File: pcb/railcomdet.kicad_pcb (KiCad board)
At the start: 4 copper layers, 90 x 70 mm, 161 parts, among them J1 MVE252-5-V, J10 MVE252-5-V, J2 MVE252-5-V, J3 MVE252-5-V, J4 MVE252-5-V, J5 MVE252-5-V, J6 PINHEADER, J7 PINHEADER, J8 PROG/DEBUG, J9 MVE252-5-V, SW1 6x6, U1 VO0631T, U10 LM339, U11 LM339, U12 STM32F103C8Tx, U13 AMS1117-3.3, U14 L78L05_SOT89, U15 SN75176AP, U2 VO0631T, U3 VO0631T, U4 L78L05_SOT89, U5 L79L05_SOT89, U6 LM339, U7 LM339, U8 LM339, U9 4052, Y1 14,7456MHz

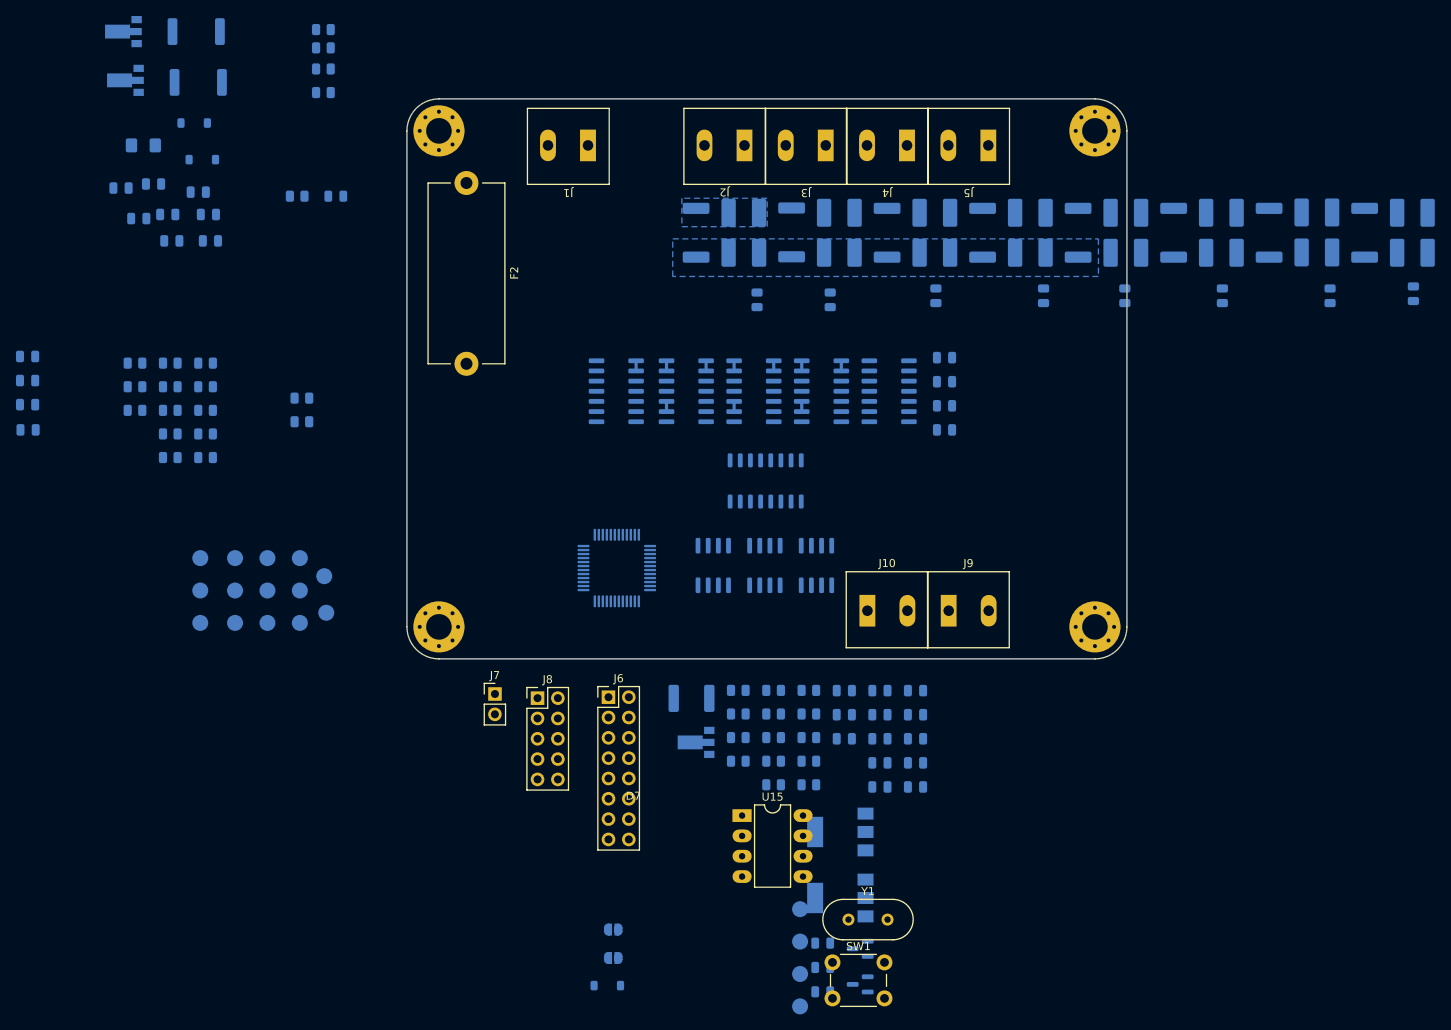
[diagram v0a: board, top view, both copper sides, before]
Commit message: pcb: wire multiplexors.
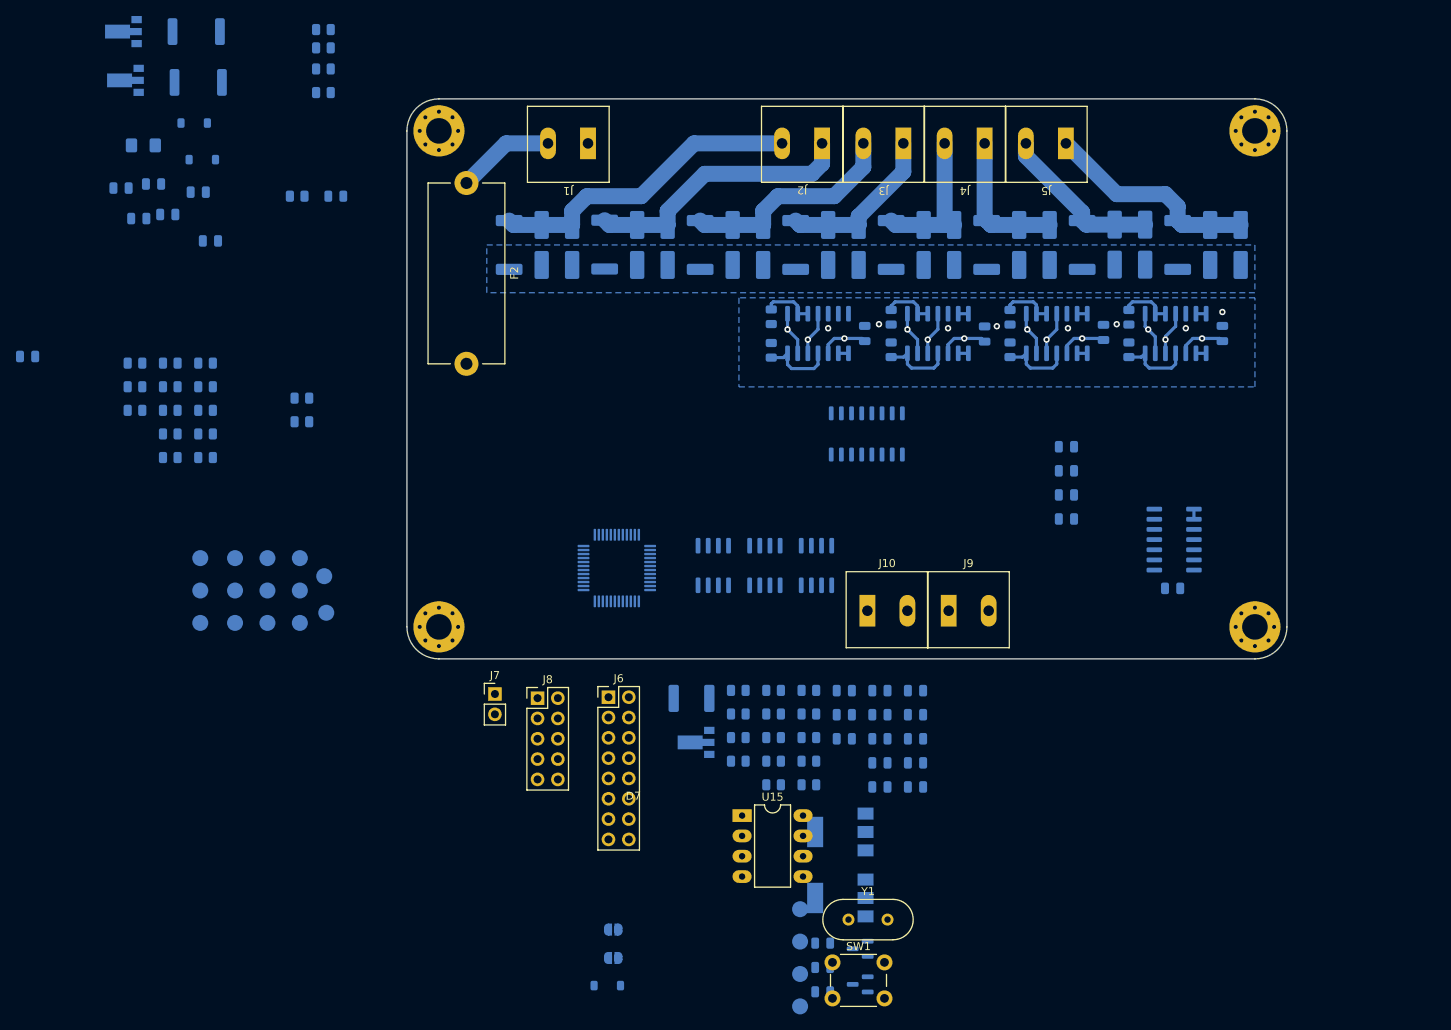
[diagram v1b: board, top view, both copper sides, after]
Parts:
- moved C15 149.6 mm to (201.9, 59.3), turned to 90 degrees
- moved C16 144.4 mm to (195.7, 91.2)
- moved C14 134.6 mm to (187.1, 59.2), turned to 90 degrees
- moved C12 102.3 mm to (172.2, 59.4), turned to 90 degrees
- moved C11 83.4 mm to (157.2, 59.3), turned to 90 degrees
- moved U11 72.1 mm to (195.9, 85.1)
- moved U10 61.6 mm to (196.1, 59.3), turned to 90 degrees
- moved U8 38.5 mm to (181.2, 59.3), turned to 90 degrees
- moved R34 35.7 mm to (190.2, 57.3), turned to 90 degrees
- moved R32 26.7 mm to (175.4, 57.3), turned to 90 degrees
- moved R33 26.0 mm to (190.2, 61.4)
- moved D19 23.4 mm to (168.4, 48.3)
- moved D24 23.4 mm to (188.5, 48.2)
- moved R16 23.4 mm to (136.7, 48.3)
- moved R14 23.4 mm to (112.8, 48.3)
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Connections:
- R29 pad 2: Net-(U8A--) -> Net-(U11A--)
- R30 pad 1: Net-(U8A--) -> Net-(U11A--)
- R31 pad 2: Net-(U10A--) -> Net-(U8A--)
- R33 pad 2: Net-(U11A--) -> Net-(U10A--)
- U10 pad 1: Net-(U9-Y3) -> Net-(U9-Y1)
- U10 pad 2: Net-(U9-Y3) -> Net-(U9-Y1)
- U11 pad 1: Net-(U9-Y1) -> /DCC/CUTOUT
- U11 pad 2: Net-(U9-Y1) -> /DCC/CUTOUT
- U8 pad 1: /DCC/CUTOUT -> Net-(U9-Y3)
- U8 pad 2: /DCC/CUTOUT -> Net-(U9-Y3)
- U8 pad 5: REF- -> REF+
- U8 pad 6: REF+ -> REF-
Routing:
- net REF-: track 0.00 -> 72.3 mm, vias 0 -> 4
- net REF+: track 0.00 -> 71.1 mm, vias 0 -> 4
- net /DCC/J1: track 0.00 -> 39.6 mm
- net /DCC/J2: track 0.00 -> 34.2 mm
- net /DCC/J3: track 0.00 -> 27.6 mm
- net /DCC/J8: track 0.00 -> 27.1 mm
- net +5VA: track 0.00 -> 24.3 mm, vias 0 -> 4
- net /DCC/J7: track 0.00 -> 20.6 mm
- net /DCC/J4: track 0.00 -> 20.6 mm
- net /DCC/J5: track 0.00 -> 18.3 mm
- net /DCC/J6: track 0.00 -> 17.9 mm
- net /DCC/J: track 0.00 -> 12.2 mm
- net /DCC/RC1: track 0.00 -> 9.28 mm
- net Net-(U8A--): track 0.00 -> 9.13 mm
- net Net-(U7A--): track 0.00 -> 9.13 mm
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- added copper zone on In1.Cu, net +5VA
- added copper zone on B.Cu, net -5VA
- added copper zone on In2.Cu, net -5VA
- removed copper zone on B.Cu, net /DCC/J1
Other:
- board size 90 x 70 mm -> 110 x 70 mm

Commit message: pcb: wire dcc voltage stabilization.
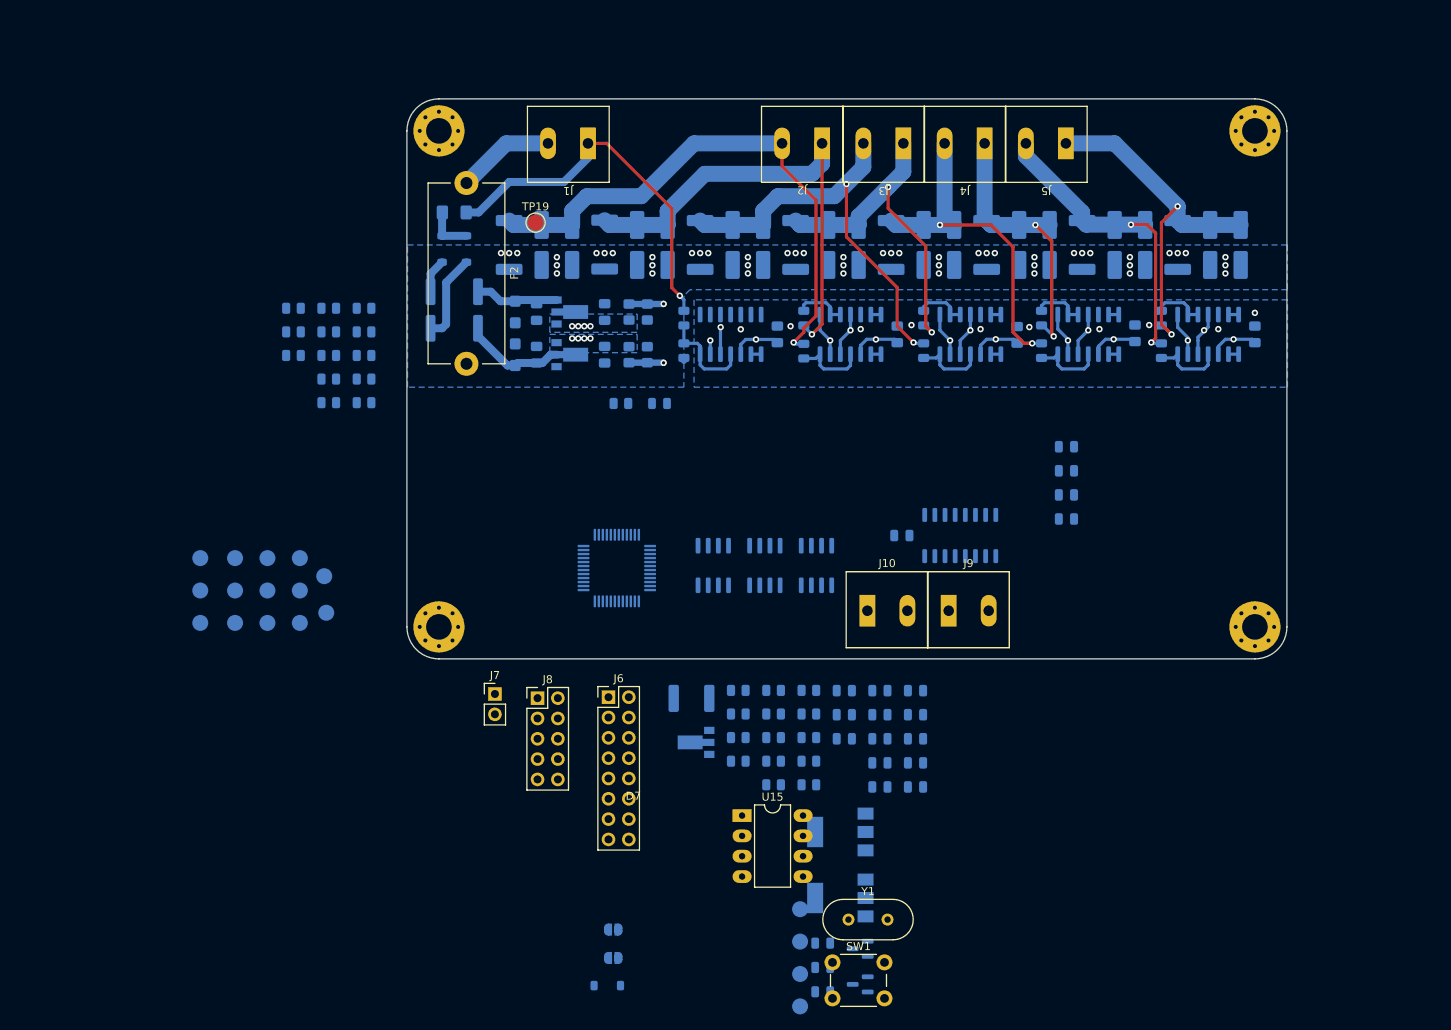
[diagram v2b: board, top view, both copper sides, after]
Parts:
- added TP19: PAD, TestPoint:TestPoint_Pad_D2.0mm, F.Cu at (116.1, 45.5)
- C10, C11, C12, C14, C15, C16, C7, C8, C9: footprint Capacitor_SMD:C_0805_2012Metric -> Capacitor_SMD:C_0805_2012Metric_Pad1.18x1.45mm_HandSolder
- C5, C6: footprint Capacitor_SMD:C_0805_2012Metric -> Capacitor_Tantalum_SMD:CP_EIA-3216-10_Kemet-I
- D1, D2: value 1N5819WS -> 1N5819
- R24, R25, R26, R27: footprint Resistor_SMD:R_0805_2012Metric -> Resistor_SMD:R_0805_2012Metric_Pad1.20x1.40mm_HandSolder
- moved C13 111.5 mm to (161.9, 84.6)
- moved U4 66.4 mm to (120.7, 56.6), turned to 0 degrees
- moved U5 65.8 mm to (120.7, 62.0), turned to 0 degrees
- moved U11 61.1 mm to (140.5, 59.4), turned to 90 degrees
- moved C16 58.7 mm to (146.3, 59.4), turned to 90 degrees
- moved C9 58.6 mm to (124.7, 56.6), turned to 90 degrees
- moved C10 57.4 mm to (124.7, 62.0), turned to 90 degrees
- moved R26 54.0 mm to (130.0, 62.0), turned to -90 degrees
- moved R25 52.2 mm to (130.0, 56.6), turned to -90 degrees
- moved R24 52.0 mm to (127.8, 56.6), turned to 90 degrees
- moved C5 51.7 mm to (113.5, 56.6), turned to -90 degrees
- moved C7 51.1 mm to (116.2, 56.6), turned to -90 degrees
- moved R27 50.3 mm to (127.8, 62.0), turned to 90 degrees
- moved R29 48.8 mm to (134.6, 57.4), turned to -90 degrees
- moved R30 48.6 mm to (134.6, 61.5), turned to -90 degrees
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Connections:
- D1 pad 2: K -> KOUT
- D2 pad 1: K -> KOUT
- F1 pad 1: K -> KOUT
- R3 pad 1: K -> KOUT
- TP6 pad 1: K -> KOUT
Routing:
- net K: track 0.00 -> 47.1 mm, vias 0 -> 1
- net REF+: track 71.1 -> 106.0 mm, vias 4 -> 6
- net /DCC/J1: track 39.6 -> 68.7 mm, vias 0 -> 1
- net REF-: track 72.3 -> 101.1 mm, vias 4 -> 6
- net /DCC/J2: track 34.2 -> 60.1 mm, vias 0 -> 1
- net /DCC/J5: track 18.3 -> 43.4 mm, vias 0 -> 2
- net /DCC/J3: track 27.6 -> 52.2 mm, vias 0 -> 2
- net /DCC/J4: track 20.6 -> 42.4 mm, vias 0 -> 2
- net /DCC/J8: track 27.1 -> 46.2 mm, vias 0 -> 2
- net /DCC/J7: track 20.6 -> 39.4 mm, vias 0 -> 2
- net /DCC/J6: track 17.9 -> 34.9 mm, vias 0 -> 2
- net Net-(U5-VI): track 0.00 -> 13.0 mm
- net Net-(U11A--): track 0.00 -> 12.3 mm
- net Net-(D2-A): track 0.00 -> 11.0 mm
- net Net-(U4-IN): track 0.00 -> 10.4 mm
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- added copper zone on B.Cu, net +5VA
- added copper zone on In2.Cu, net GNDA

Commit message: pcb: wire multiplexer's inputs.
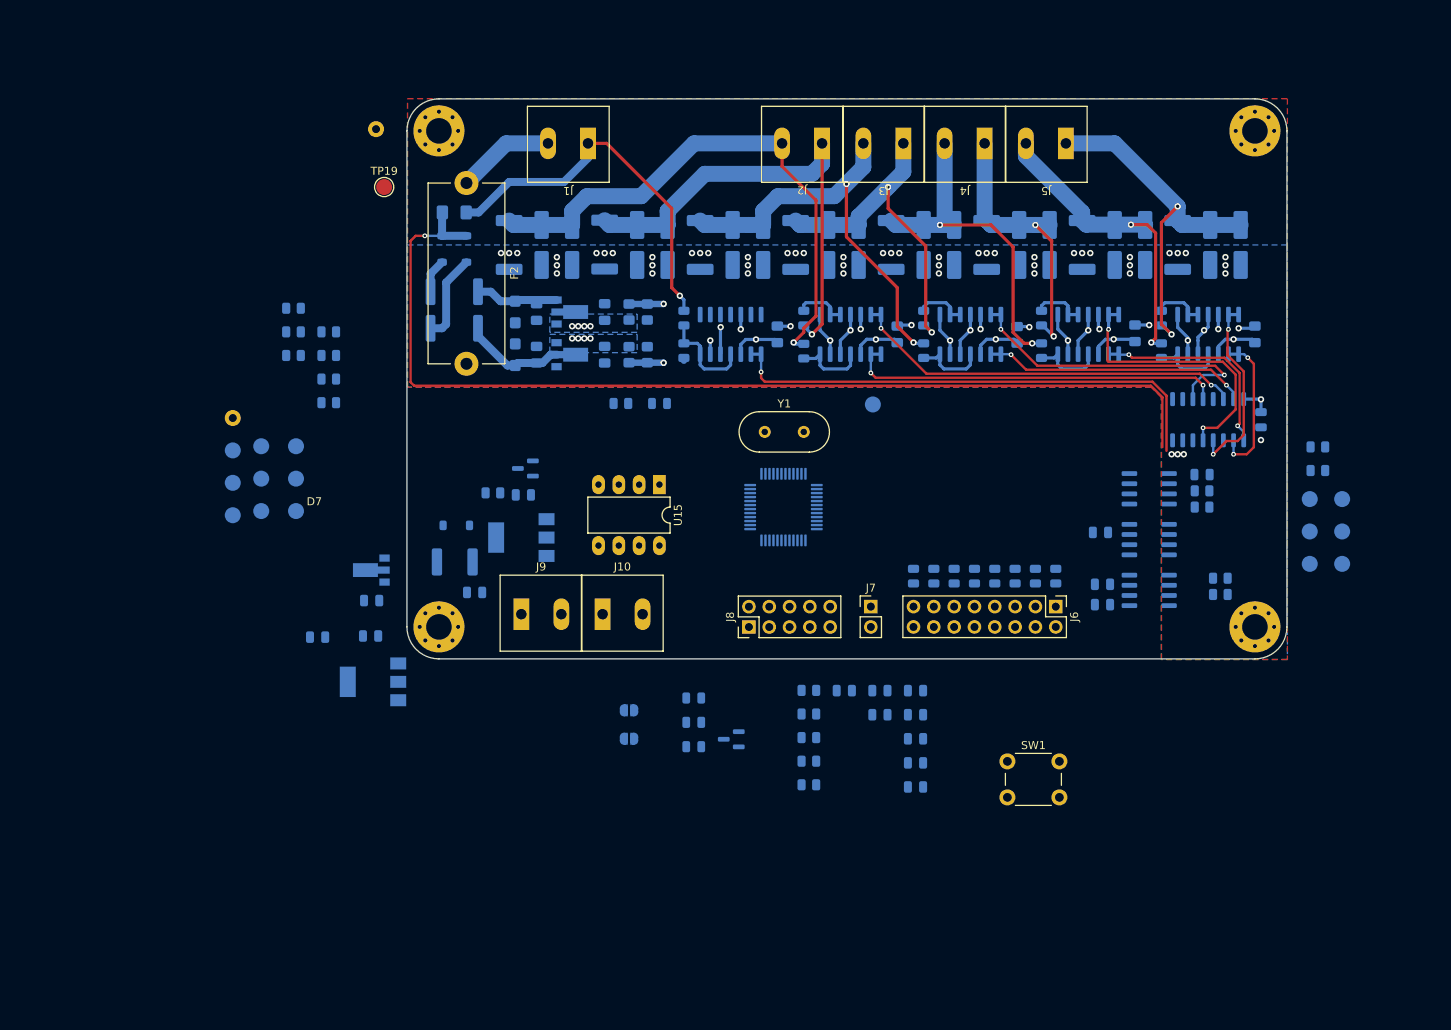
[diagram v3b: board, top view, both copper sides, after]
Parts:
- TP14, TP15: value PAD -> RING; footprint TestPoint:TestPoint_Pad_D2.0mm -> TestPoint:TestPoint_Loop_D1.80mm_Drill1.0mm_Beaded
- moved TP4 130.5 mm to (212.9, 80.0)
- moved TP5 130.5 mm to (212.9, 84.1)
- moved TP6 130.5 mm to (212.9, 88.1)
- moved TP1 130.5 mm to (216.9, 80.0)
- moved TP2 130.5 mm to (216.9, 84.1)
- moved TP3 130.5 mm to (216.9, 88.1)
- moved R4 119.5 mm to (213.9, 73.5)
- moved R5 119.5 mm to (213.9, 76.5)
- moved R6 116.4 mm to (201.7, 89.9)
- moved R1 112.9 mm to (201.7, 91.9)
- moved R2 106.6 mm to (199.4, 79.0)
- moved R3 106.5 mm to (199.4, 81.0)
- moved TP15 93.8 mm to (78.2, 69.9)
- moved TP16 93.8 mm to (78.2, 73.9)
- moved TP17 93.8 mm to (78.2, 78.0)
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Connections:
- C1 pad 1: +5V -> +5VA
- C1 pad 2: GND -> GNDA
- U10 pad 1: Net-(U9-Y1) -> Net-(U9-Y2)
- U10 pad 13: Net-(U9-Y0) -> Net-(U9-Y3)
- U10 pad 14: Net-(U9-Y0) -> Net-(U9-Y3)
- U10 pad 2: Net-(U9-Y1) -> Net-(U9-Y2)
- U8 pad 1: Net-(U9-Y3) -> Net-(U9-Y0)
- U8 pad 13: Net-(U9-Y2) -> Net-(U9-Y1)
- U8 pad 14: Net-(U9-Y2) -> Net-(U9-Y1)
- U8 pad 2: Net-(U9-Y3) -> Net-(U9-Y0)
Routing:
- net KOUT: track 5.99 -> 128.8 mm, vias 0 -> 1
- net /DCC/CUTOUT: track 1.27 -> 62.7 mm, vias 0 -> 1
- net Net-(U9-X1): track 1.27 -> 49.9 mm, vias 0 -> 2
- net Net-(U9-X0): track 1.27 -> 47.5 mm, vias 0 -> 2
- net Net-(U9-X3): track 1.27 -> 39.6 mm, vias 0 -> 2
- net Net-(U9-Y1): track 1.27 -> 34.7 mm, vias 0 -> 2
- net Net-(U9-X2): track 1.27 -> 33.2 mm, vias 0 -> 2
- net Net-(U9-Y0): track 1.27 -> 26.2 mm, vias 0 -> 2
- net Net-(U9-Y3): track 1.27 -> 23.8 mm, vias 0 -> 2
- net -5VA: track 0.05 -> 18.2 mm
- net Net-(U9-Y2): track 1.27 -> 18.7 mm, vias 0 -> 2
- net REF-: track 101.1 -> 106.8 mm
- net +5VA: track 30.5 -> 34.3 mm, vias 9 -> 10
- net GNDA: vias 48 -> 52
- added copper zone on F.Cu, net GNDA
